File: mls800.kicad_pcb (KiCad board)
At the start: 2 copper layers, 293.4 x 80.5 mm, 106 parts, among them CON1 BARREL_JACK, IC1 6N137, J1 USB, J10 NSJ8HC, J11 NRJ4HF-1, J2 NRJ4HF-1, J3 NSJ8HC, J4 NSJ8HC, J5 NSJ8HC, J6 NSJ8HC, J7 NSJ8HC, J8 NSJ8HC, J9 NSJ8HC, P1 CONN_02X03, P2 DIN_5, P3 DIN_5, P4 CONN_02X03, P5 CONN_02X03, SW10 SW_TACT_LED, SW11 SW_TACT_LED, SW12 SW_PUSH_RIGHT_ANGLE, SW2 SW_TACT_LED, SW3 SW_TACT_LED, SW4 SW_TACT_LED, SW5 SW_TACT_LED, SW6 SW_TACT_LED, SW7 SW_TACT_LED, SW8 SW_TACT_LED, SW9 SW_TACT_LED, U1 LM340MP-5.0/NOPB, U2 ATmega32U4-AU, U3 24LC256, U4 MCP23017, U5 AS1115, U6 ULN2803A, U7 ULN2803A, U8 LM340MP-5.0/NOPB, X1 16Mhz

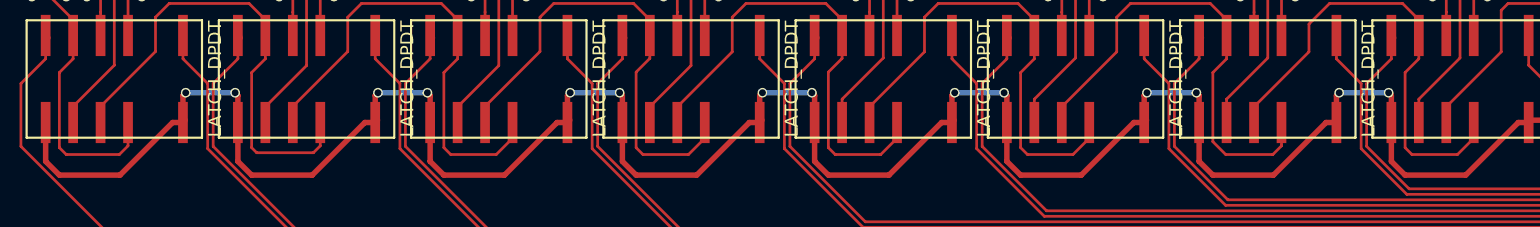
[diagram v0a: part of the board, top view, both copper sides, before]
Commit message: Optimized relays nets to allow copper planes to be filled
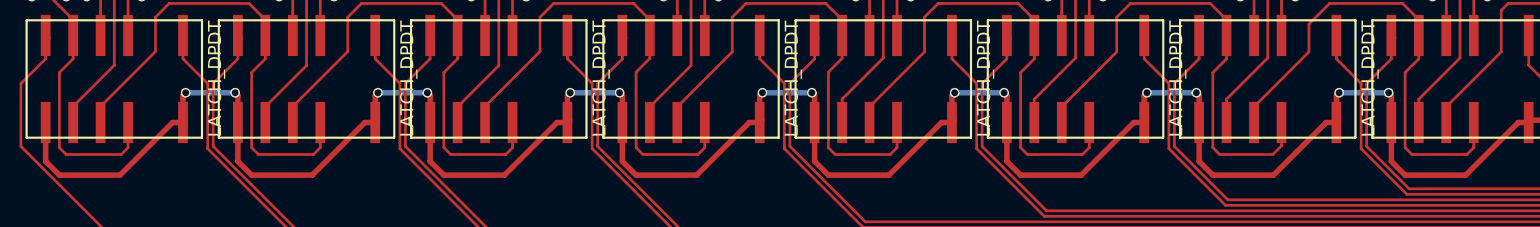
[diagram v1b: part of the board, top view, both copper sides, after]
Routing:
- net Net-(RE7-Pad9): track 43.8 -> 44.3 mm
- net Net-(RE5-Pad9): track 44.2 -> 44.7 mm
- net Net-(RE3-Pad9): track 44.2 -> 44.7 mm
- net Net-(RE2-Pad9): track 44.2 -> 44.7 mm
- net Net-(RE4-Pad9): track 44.2 -> 44.7 mm

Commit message: Repositionned all elements on a 1.27mm grid
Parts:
- moved R5 23.0 mm to (97.8, 110.5)
- moved R8 16.3 mm to (97.8, 105.4)
- moved P5 1.27 mm to (179.1, 119.4)
- moved AFF1 0.25 mm to (127.0, 113.0)
- moved MH 0.25 mm to (64.8, 104.1)
- moved MH 0.25 mm to (317.5, 104.1)
- moved SW10 0.25 mm to (85.1, 113.0)
- moved SW11 0.25 mm to (68.6, 113.0)
- moved SW2 0.25 mm to (196.8, 113.0)
- moved SW3 0.25 mm to (213.4, 113.0)
- moved SW4 0.25 mm to (229.9, 113.0)
- moved SW5 0.25 mm to (246.4, 113.0)
- moved SW6 0.25 mm to (262.9, 113.0)
- moved SW7 0.25 mm to (279.4, 113.0)
- moved SW8 0.25 mm to (295.9, 113.0)
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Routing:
- net /Front panel/SEGD: track 220.2 -> 0.36 mm, vias 1 -> 0
- net /Front panel/SEGE: track 218.6 -> 0.00 mm, vias 1 -> 0
- net /Front panel/SEGG: track 198.4 -> 0.00 mm
- net /Front panel/SEGF: track 192.2 -> 0.00 mm, vias 4 -> 0
- net Net-(SW2-Pad1): track 173.9 -> 0.00 mm, vias 2 -> 0
- net /Front panel/LEDS: track 158.0 -> 0.00 mm, vias 2 -> 0
- net /Front panel/SEGC: track 135.5 -> 0.00 mm, vias 2 -> 0
- net VDD: track 118.3 -> 0.74 mm, vias 3 -> 0
- net /Front panel/SEGB: track 114.4 -> 0.00 mm, vias 4 -> 0
- net /Front panel/SEGA: track 112.7 -> 0.00 mm, vias 4 -> 0
- net /Front panel/EDIT_LED: track 92.3 -> 0.00 mm
- net /Front panel/SEGDP: track 88.2 -> 0.00 mm, vias 2 -> 0
- net Net-(SW10-Pad1): track 83.7 -> 0.00 mm, vias 2 -> 0
- net /Front panel/DIG1: track 48.0 -> 0.00 mm
- net /Front panel/DIG2: track 39.2 -> 0.00 mm
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
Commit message: Front panel routing
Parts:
- moved R5 23.0 mm to (74.9, 113.0)
- moved R8 9.92 mm to (91.4, 113.0)
- moved C16 2.54 mm to (163.8, 120.7), turned to 270 degrees
- moved C13 1.80 mm to (172.7, 120.7), turned to 0 degrees
- moved R7 1.80 mm to (172.7, 118.1), turned to 180 degrees
- moved U5 1.27 mm to (157.5, 113.0)
- moved R19 0.25 mm to (153.7, 119.4)
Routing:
- net Net-(SW2-Pad1): track 0.00 -> 172.2 mm
- net /Front panel/LEDS: track 0.00 -> 156.4 mm
- net /Front panel/SEGD: track 0.36 -> 58.9 mm
- net /Front panel/SEGE: track 0.00 -> 58.5 mm, vias 0 -> 1
- net /Front panel/SEGDP: track 0.00 -> 55.3 mm
- net /Front panel/SEGC: track 0.00 -> 54.1 mm
- net /Front panel/SEGG: track 0.00 -> 48.3 mm
- net /Front panel/IRQ: track 0.16 -> 22.7 mm
- net VDD: track 0.74 -> 17.1 mm
- net /Front panel/SEGF: track 0.00 -> 12.5 mm
- net /Front panel/SEGB: track 0.00 -> 12.5 mm
- net /Front panel/SEGA: track 0.00 -> 12.5 mm
- net Net-(R19-Pad1): track 0.00 -> 2.53 mm
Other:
- board size 293.4 x 80.5 mm -> 454.7 x 81.8 mm

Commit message: Front panel routing
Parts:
- turned R8 to 90 degrees
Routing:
- net /Front panel/SEGF: track 12.5 -> 189.7 mm, vias 0 -> 4
- net /Front panel/SEGD: track 58.9 -> 222.0 mm, vias 0 -> 4
- net /Front panel/SEGE: track 58.5 -> 219.7 mm, vias 1 -> 3
- net /Front panel/SEGG: track 48.3 -> 200.8 mm
- net /Front panel/SEGB: track 12.5 -> 119.4 mm, vias 0 -> 4
- net VDD: track 17.1 -> 111.8 mm, vias 0 -> 2
- net /Front panel/EDIT_LED: track 0.00 -> 93.9 mm, vias 0 -> 1
- net /Front panel/SEGA: track 12.5 -> 106.1 mm, vias 0 -> 4
- net /Front panel/SEGC: track 54.1 -> 139.5 mm
- net Net-(SW10-Pad1): track 0.00 -> 81.6 mm, vias 0 -> 2
- net /Front panel/DIG1: track 0.00 -> 46.5 mm
- net /Front panel/DIG2: track 0.00 -> 37.7 mm
- net /Front panel/SCL: track 0.00 -> 34.6 mm, vias 0 -> 1
- net /Front panel/DIG3: track 0.00 -> 34.1 mm
- net /Front panel/DIG4: track 0.00 -> 33.5 mm, vias 0 -> 1
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
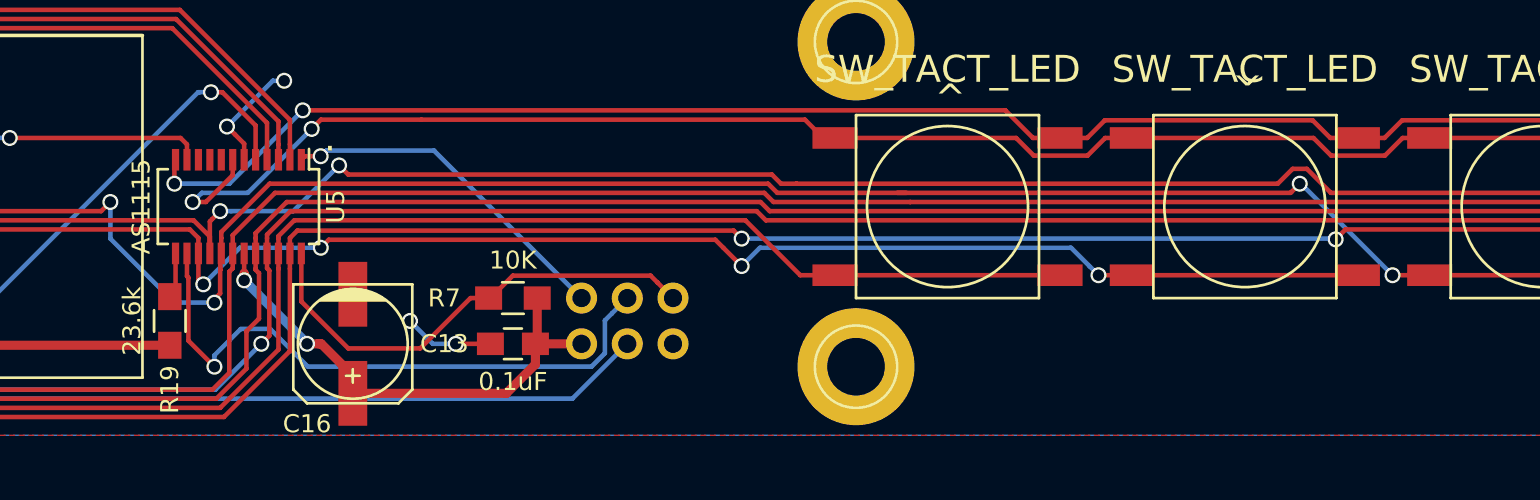
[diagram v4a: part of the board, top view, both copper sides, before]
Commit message: Front panel routing & warnings
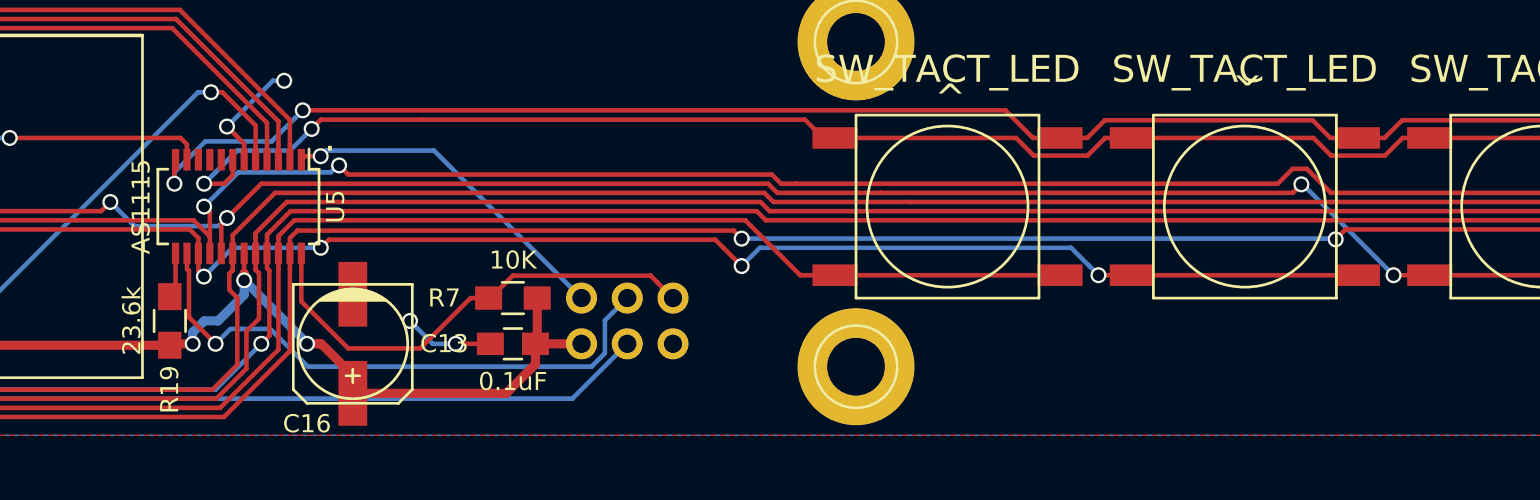
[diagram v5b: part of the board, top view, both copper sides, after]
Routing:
- net VDD: track 111.8 -> 118.2 mm, vias 2 -> 3
- net /Front panel/SEGB: track 119.4 -> 114.1 mm
- net /Front panel/SCL: track 34.6 -> 32.4 mm
- net /Front panel/LEDS: track 163.2 -> 161.1 mm
- net /Front panel/SEGA: track 106.1 -> 105.4 mm

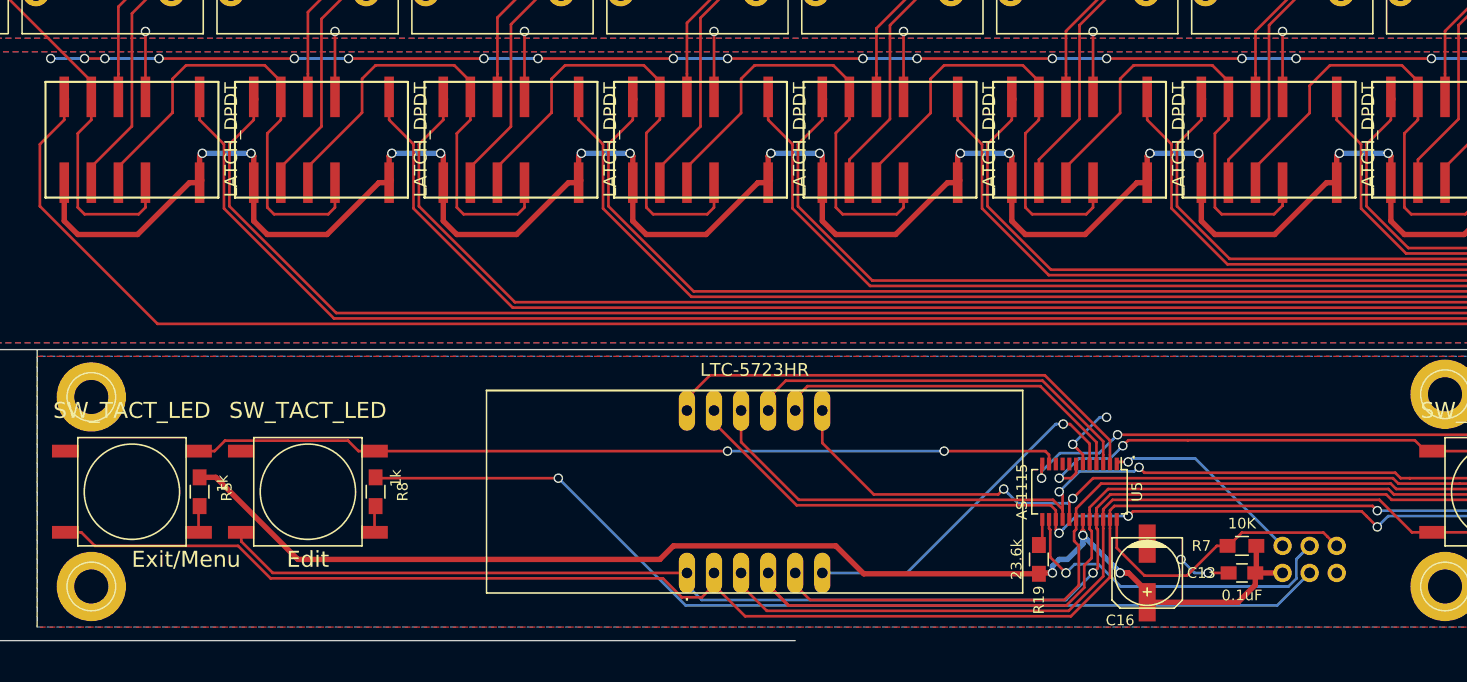
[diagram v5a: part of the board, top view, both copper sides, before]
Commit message: Front panel routing
Fixed motherboard copper plane on the right side of relays
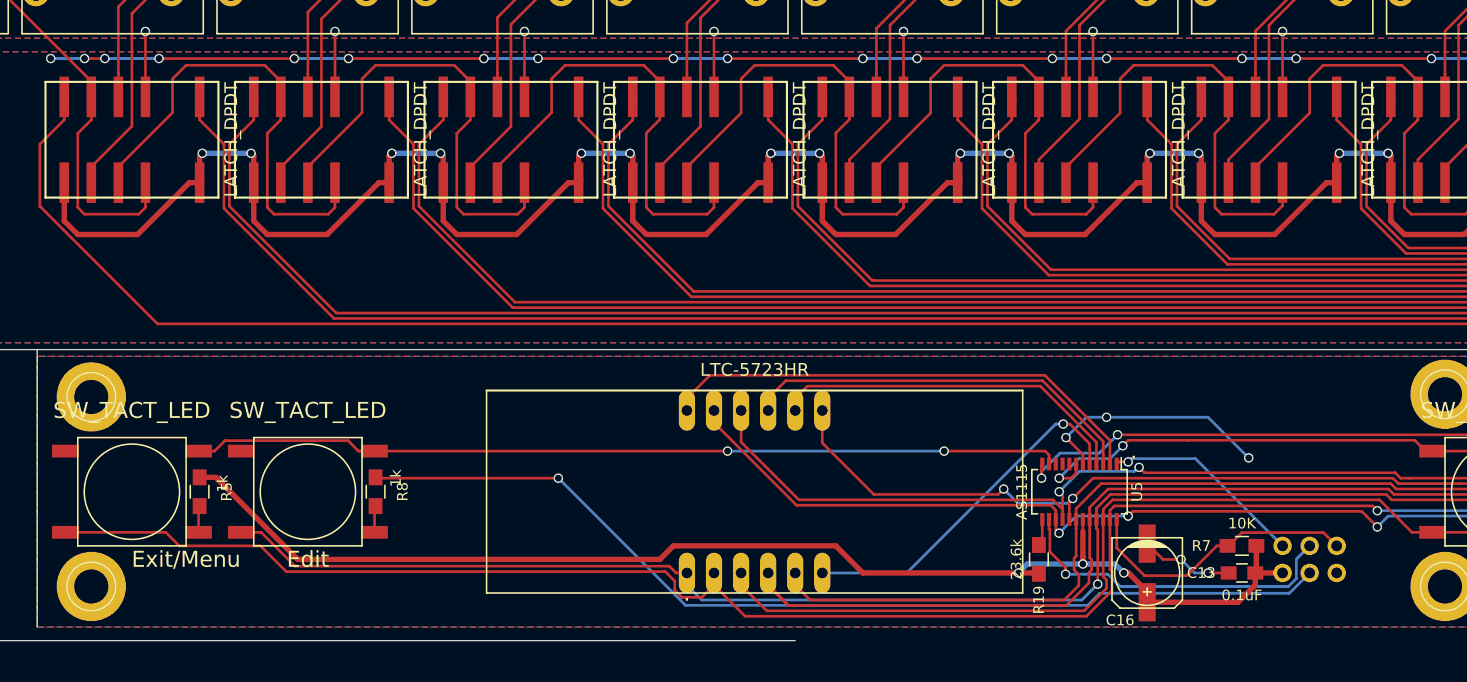
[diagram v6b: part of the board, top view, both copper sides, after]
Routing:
- net /Front panel/DGND: track 11.5 -> 31.4 mm, vias 4 -> 5
- net VDD: track 118.2 -> 122.4 mm
- net /Front panel/SEGD: track 222.0 -> 223.5 mm
- net /Front panel/SEGDP: track 88.8 -> 89.9 mm
- net /Front panel/SCL: track 32.4 -> 31.8 mm
